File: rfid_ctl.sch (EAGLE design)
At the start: 39 parts, among them Q1 FDS5680, Q2 FDS5680, SW2 L202011MS02Q, U1 MC34063SMD, X2 1503_02

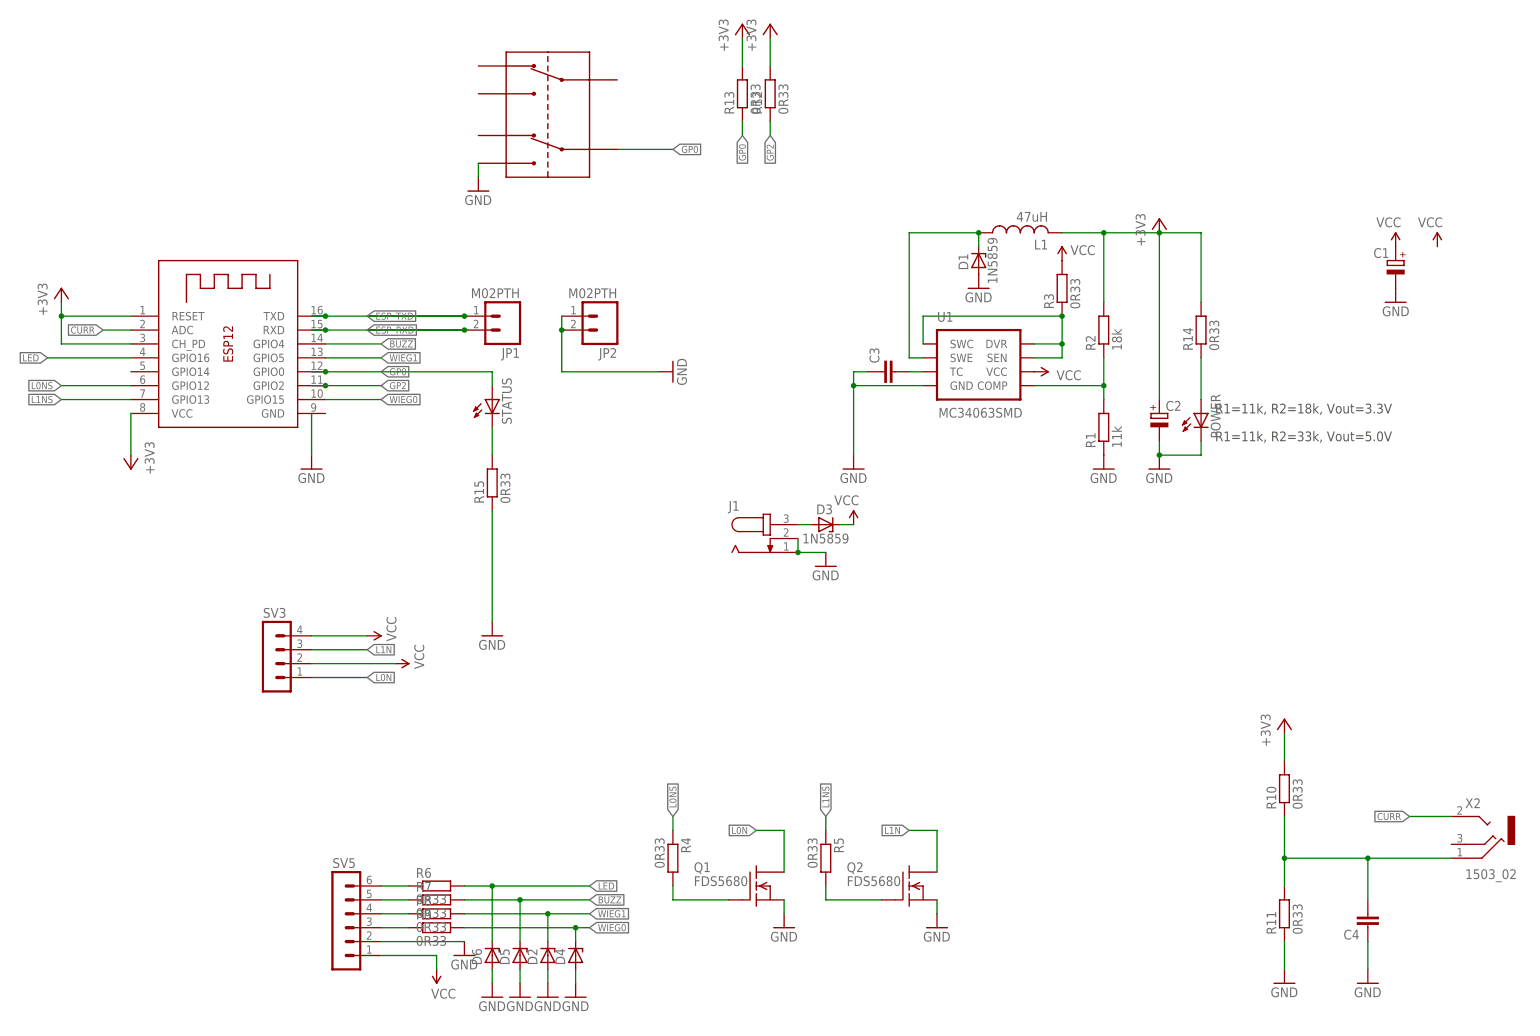
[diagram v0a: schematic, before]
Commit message: GPIO pulled low and HP jack swapped with something sourcable
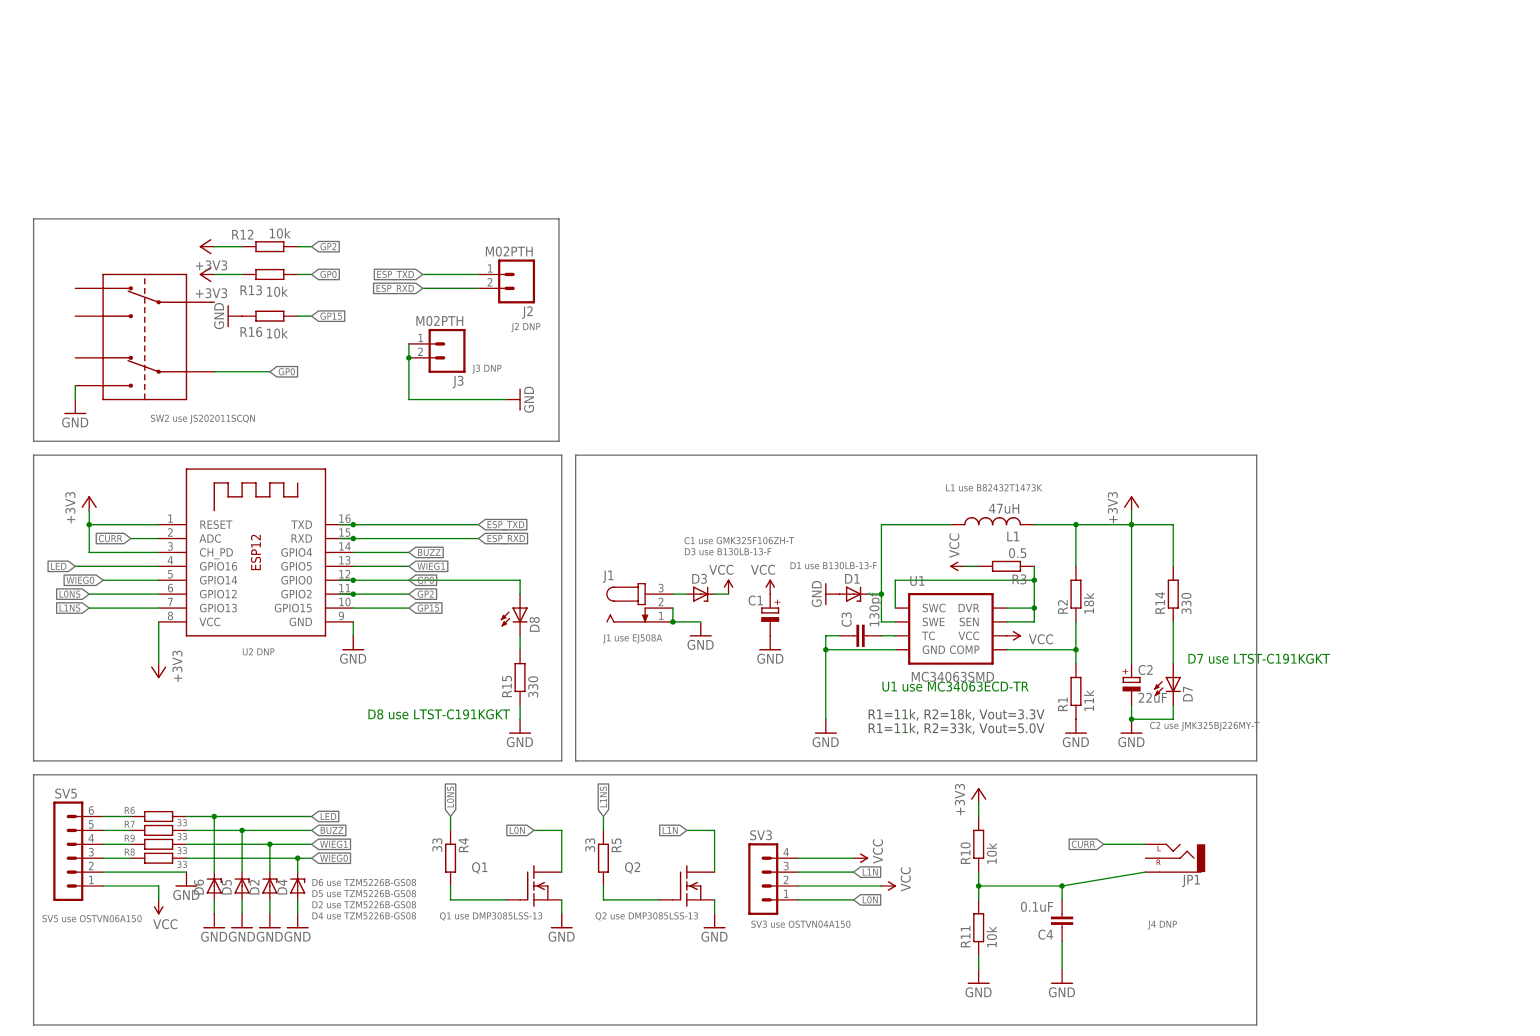
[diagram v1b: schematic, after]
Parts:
- removed JP2: M02PTH, SparkFun-Connectors:M02PTH
- removed POWER, STATUS: (no value), adafruit:LEDCHIP-LED0603
- removed X1: (no value), adafruit:ESP-12
- removed X2: 1503_02, con-lumberg:1503_02
- added D7, D8: (no value), adafruit:LEDCHIP-LED0603
- added J2, J3: M02PTH, SparkFun-Connectors:M02PTH
- added R16: 10k, rcl:R-EU_R0603
- added U2: (no value), adafruit:ESP-12
- C2: value (none) -> 22uF
- C3: value (none) -> 130pf
- C4: value (none) -> 0.1uF
- D1, D2, D3, D4, D5, D6: value 1N5859 -> (none)
- JP1: value M02PTH -> (none); device SparkFun-Connectors:M02PTH -> SparkFun-Connectors:AUDIO-JACKSMD2
- R10, R11, R12, R13: value 0R33 -> 10k
- R14, R15: value 0R33 -> 330
- R3: value 0R33 -> 0.5
- R4, R5, R6, R7, R8, R9: value 0R33 -> 33
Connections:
- new net GP15: R16.1, U2.GPIO15
- net +3V3: now also U2.CH_PD, U2.RESET, U2.VCC; no longer X1.CH_PD, X1.RESET, X1.VCC
- net BUZZ: now also U2.GPIO4; no longer X1.GPIO4
- net CURR: now also JP1.LEFT, U2.ADC; no longer X1.ADC, X2.2
- net ESP_RXD: now also J2.2, U2.RXD; no longer JP1.2, X1.RXD
- net ESP_TXD: now also J2.1, U2.TXD; no longer JP1.1, X1.TXD
- net GND: now also D7.C, J3.1, J3.2, R16.2, U2.GND; no longer JP2.1, JP2.2, POWER.C
- net GP0: now also D8.A, U2.GPIO0; no longer STATUS.A, X1.GPIO0
- net GP2: now also U2.GPIO2; no longer X1.GPIO2
- net L0NS: now also U2.GPIO12; no longer X1.GPIO12
- net L1NS: now also U2.GPIO13; no longer X1.GPIO13
- net LED: now also U2.GPIO16; no longer X1.GPIO16
- net N$12: now also JP1.SLEEVE; no longer X2.1
- net N$13: now also D7.A; no longer POWER.A
- net N$14: now also D8.C; no longer STATUS.C
- net WIEG0: now also U2.GPIO14; no longer X1.GPIO15
- net WIEG1: now also U2.GPIO5; no longer X1.GPIO5
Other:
- note added: "C1 use GMK325F106ZH-T"
- note added: "C2 use JMK325BJ226MY-T"
- note added: "D1 use B130LB-13-F"
- note added: "D2 use TZM5226B-GS08"
- note added: "D3 use B130LB-13-F"
- note added: "D4 use TZM5226B-GS08"
- note added: "D5 use TZM5226B-GS08"
- note added: "D6 use TZM5226B-GS08"
- note added: "D7 use LTST-C191KGKT"
- note added: "D8 use LTST-C191KGKT"
- note added: "J1 use EJ508A"
- note added: "J2 DNP"
- note added: "J3 DNP"
- note added: "J4 DNP"
- note added: "L1 use B82432T1473K"
- note added: "Q1 use DMP3085LSS-13"
- note added: "Q2 use DMP3085LSS-13"
- note added: "SV3 use OSTVN04A150"
- note added: "SV5 use OSTVN06A150"
- note added: "SW2 use JS202011SCQN"
- note added: "U1 use MC34063ECD-TR"
- note added: "U2 DNP"
- moved on the sheet: C1, C2, C3, C4, D1, D2, D3, D4, D5, D6, J1, L1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
